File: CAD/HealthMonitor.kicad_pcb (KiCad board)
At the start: 2 copper layers, 20 x 30 mm, 28 parts, among them J1 USB_C_Receptacle_USB2.0, U1 ADP5092ACPZ-1-R7, U2 LTC4079IDD-PBF

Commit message: Finished PCB Draft -- waiting for review
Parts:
- added C10: 10µF, Capacitor_SMD:C_0402_1005Metric, F.Cu at (125.1, 111.9)
- added C11: 0.1µF, Capacitor_SMD:C_0402_1005Metric, F.Cu at (119.1, 118.9)
- added C12: 4.7µF, Capacitor_SMD:C_0402_1005Metric, F.Cu at (115.3, 117.0)
- added C13: 0.1µF, Capacitor_SMD:C_0402_1005Metric, F.Cu at (124.1, 120.1)
- added C14: 5600pF, Capacitor_SMD:C_0402_1005Metric, F.Cu at (122.3, 117.5)
- added C15: 10µF 10V, Capacitor_SMD:C_0402_1005Metric, F.Cu at (117.0, 123.0)
- added C16: 4.7µF, Capacitor_SMD:C_0402_1005Metric, F.Cu at (123.4, 118.6)
- added C17: 22u, Capacitor_SMD:C_0603_1608Metric, B.Cu at (105.0, 123.8)
- added C18: 12p, Capacitor_SMD:C_0402_1005Metric, F.Cu at (105.6, 107.6)
- added C19: 12p, Capacitor_SMD:C_0402_1005Metric, F.Cu at (105.6, 109.1)
- added C20: 1u, Capacitor_SMD:C_0402_1005Metric, F.Cu at (125.5, 105.4)
- added C21: 1u, Capacitor_SMD:C_0402_1005Metric, B.Cu at (115.6, 106.7)
- added C22: 0.1u, Capacitor_SMD:C_0402_1005Metric, B.Cu at (116.7, 106.7)
- added C23: 1u, Capacitor_SMD:C_0402_1005Metric, B.Cu at (112.8, 110.3)
- added C24: 1u, Capacitor_SMD:C_0402_1005Metric, F.Cu at (153.9, 126.5)
- added C25: 1u, Capacitor_SMD:C_0402_1005Metric, F.Cu at (153.2, 121.5)
- added C26: 1µf 10V, Capacitor_SMD:C_0402_1005Metric, F.Cu at (115.0, 120.2)
- added C27: 22u, Capacitor_SMD:C_0603_1608Metric, B.Cu at (105.0, 114.0)
- added C6: 4.7u, Capacitor_SMD:C_0402_1005Metric, F.Cu at (147.5, 106.8)
- added C7: 1u, Capacitor_SMD:C_0402_1005Metric, B.Cu at (118.9, 100.3)
- added C9: 100nF, Capacitor_SMD:C_0402_1005Metric, F.Cu at (125.1, 110.0)
- added D1: LED_ir, Diode_SMD:D_0603_1608Metric, B.Cu at (116.6, 103.9)
- added D2: LED_green, Diode_SMD:D_0603_1608Metric, B.Cu at (112.7, 100.9)
- added D3: LED_green, Diode_SMD:D_0603_1608Metric, B.Cu at (120.3, 100.9)
- added D4: SML-LX0404SIUPGUSB, SML-LX0404SIUPGUSB:DIOC0404X01-4N, F.Cu at (127.4, 105.5)
- added D5: LED-LT PWSG-AABB-36-46-F, LED_SMD:LED_PLCC-2, B.Cu at (108.4, 114.0)
- added D6: VEMD5010X01, footprints:VEMD5010X01, B.Cu at (106.1, 119.0)
- added D7: LED_LY_P47F-TM, LED_SMD:LED_PLCC-2, B.Cu at (108.4, 123.8)
- added D8: VEMD5010X01, footprints:VEMD5010X01, B.Cu at (110.6, 119.0)
- added J10: SDA, Connector_PinHeader_1.27mm:PinHeader_1x01_P1.27mm_Vertical, F.Cu at (141.9, 111.7)
- added J11: SCL, Connector_PinHeader_1.27mm:PinHeader_1x01_P1.27mm_Vertical, F.Cu at (141.9, 110.2)
- added J12: DIS_SW, Connector_PinHeader_1.27mm:PinHeader_1x01_P1.27mm_Vertical, F.Cu at (141.9, 113.0)
- added J13: BAT_CHRG, Connector_PinHeader_1.27mm:PinHeader_1x01_P1.27mm_Vertical, F.Cu at (141.9, 114.5)
- added J14: USBDP, Connector_PinHeader_1.27mm:PinHeader_1x01_P1.27mm_Vertical, F.Cu at (143.8, 115.2)
- added J15: USBDM, Connector_PinHeader_1.27mm:PinHeader_1x01_P1.27mm_Vertical, F.Cu at (143.8, 116.5)
- added J16: USB_V, Connector_PinHeader_1.27mm:PinHeader_1x01_P1.27mm_Vertical, F.Cu at (141.9, 115.8)
- added J17: VBUS, Connector_PinHeader_1.27mm:PinHeader_1x01_P1.27mm_Vertical, F.Cu at (129.0, 114.2)
- added J18: D+, Connector_PinHeader_1.27mm:PinHeader_1x01_P1.27mm_Vertical, F.Cu at (129.0, 115.6)
- added J19: D-, Connector_PinHeader_1.27mm:PinHeader_1x01_P1.27mm_Vertical, F.Cu at (129.0, 117.0)
- added J2: TEG+, Connector_PinHeader_1.27mm:PinHeader_1x01_P1.27mm_Vertical, F.Cu at (141.9, 100.5)
- added J20: SDA, Connector_PinHeader_1.27mm:PinHeader_1x01_P1.27mm_Vertical, F.Cu at (129.0, 110.0)
- added J21: SCL, Connector_PinHeader_1.27mm:PinHeader_1x01_P1.27mm_Vertical, F.Cu at (129.0, 108.6)
- added J22: VCC, Connector_PinHeader_1.27mm:PinHeader_1x01_P1.27mm_Vertical, F.Cu at (130.3, 106.7)
- added J23: GND, Connector_PinHeader_1.27mm:PinHeader_1x01_P1.27mm_Vertical, F.Cu at (130.3, 105.3)
- added J24: BAT_CHRG, Connector_PinHeader_1.27mm:PinHeader_1x01_P1.27mm_Vertical, F.Cu at (129.0, 112.8)
- added J25: DIS_SW, Connector_PinHeader_1.27mm:PinHeader_1x01_P1.27mm_Vertical, F.Cu at (129.0, 111.4)
- added J3: TEG-, Connector_PinHeader_1.27mm:PinHeader_1x01_P1.27mm_Vertical, F.Cu at (141.9, 101.8)
- added J4: BAT-, Connector_PinHeader_1.27mm:PinHeader_1x01_P1.27mm_Vertical, F.Cu at (141.9, 106.0)
- added J5: BAT+, Connector_PinHeader_1.27mm:PinHeader_1x01_P1.27mm_Vertical, F.Cu at (141.9, 103.2)
- added J6: USB_C_Receptacle_USB2.0, Connector_USB:USB_C_Receptacle_Amphenol_12401610E4-2A_CircularHoles, F.Cu at (144.9, 123.0)
- added J7: Conn_02x05_Odd_Even, Connector_PinHeader_1.27mm:PinHeader_2x05_P1.27mm_Vertical, F.Cu at (127.0, 98.0)
- added J8: VCC, Connector_PinHeader_1.27mm:PinHeader_1x01_P1.27mm_Vertical, F.Cu at (141.9, 108.8)
- added J9: GND, Connector_PinHeader_1.27mm:PinHeader_1x01_P1.27mm_Vertical, F.Cu at (141.9, 107.5)
- added L2: 4.7µH, Inductor_SMD:L_0603_1608Metric, F.Cu at (122.9, 116.1)
- added R19: 3.32M, Resistor_SMD:R_0402_1005Metric, F.Cu at (156.2, 107.6)
- added R20: 2.4k, Resistor_SMD:R_0402_1005Metric, F.Cu at (151.9, 116.7)
- added R21: 6.65M, Resistor_SMD:R_0402_1005Metric, F.Cu at (158.2, 107.6)
- added R22: 412k, Resistor_SMD:R_0402_1005Metric, F.Cu at (151.9, 118.2)
- added R23: 10k, Resistor_SMD:R_0402_1005Metric, B.Cu at (117.0, 99.0)
- added R24: 10k, Resistor_SMD:R_0402_1005Metric, B.Cu at (117.0, 97.8)
- added R25: 10k, Resistor_SMD:R_0402_1005Metric, B.Cu at (114.1, 100.4)
- added R26: 50k, Resistor_SMD:R_0402_1005Metric, F.Cu at (121.4, 118.6)
- added R27: 50k, Resistor_SMD:R_0402_1005Metric, F.Cu at (125.4, 121.0)
- added R28: 50k, Resistor_SMD:R_0402_1005Metric, F.Cu at (124.3, 122.5)
- added R29: 50k, Resistor_SMD:R_0402_1005Metric, F.Cu at (123.1, 122.9)
- added R30: 50k, Resistor_SMD:R_0402_1005Metric, F.Cu at (122.0, 123.0)
- added R31: 4.75k, Resistor_SMD:R_0402_1005Metric, F.Cu at (120.8, 117.0)
- added R32: 10k, Resistor_SMD:R_0402_1005Metric, F.Cu at (105.3, 105.4)
- added R33: 10k, Resistor_SMD:R_0402_1005Metric, F.Cu at (104.5, 98.3)
- added R34: 6.6k, Resistor_SMD:R_0402_1005Metric, F.Cu at (127.5, 106.8)
- added R35: 10k, Resistor_SMD:R_0402_1005Metric, F.Cu at (147.3, 111.1)
- added R36: 0, Resistor_SMD:R_0603_1608Metric, F.Cu at (130.9, 108.8)
- added Rpu1: 10kOhms, Resistor_SMD:R_0402_1005Metric, F.Cu at (123.6, 107.7)
- added Rpu2: 10kOhms, Resistor_SMD:R_0402_1005Metric, F.Cu at (122.6, 107.7)
- added U10: AT24CS02-XHM, Package_SO:TSSOP-8_4.4x3mm_P0.65mm, F.Cu at (106.9, 100.8)
- added U11: BT832L, footprints:BT832-BT832L, F.Cu at (109.8, 106.2)
- added U12: CP2102N-A01-GQFN24, Package_DFN_QFN:QFN-24-1EP_4x4mm_P0.5mm_EP2.6x2.6mm, B.Cu at (116.8, 110.4)
- added U13: ADG884BRMZ, footprints:ADG884BRMZ, F.Cu at (149.8, 113.6)
- added U3: LTC4079IDD-PBF, footprints:LTC4079IDD-PBF, F.Cu at (155.4, 118.5)
- added U4: LD39015M33R, Package_TO_SOT_SMD:SOT-23-5, F.Cu at (153.4, 124.0)
- added U5: BH1792GLC, BH1790GLC-E2:PQFN70P280X280X100-10N, B.Cu at (116.5, 101.1)
- added U6: LSM6DS33TR, LSM6DS33TR:PQFN50P300X300X86-16N, F.Cu at (122.7, 110.8)
- added U7: TXB0104RUT, Package_DFN_QFN:Texas_R_PUQFN-N12, F.Cu at (120.3, 120.6)
- added U8: MAX1921EUT18+, footprints:MAX1921EUT18&plus_T, F.Cu at (118.0, 116.5)
- added U9: MAX86141ENP+, footprints:MAX86141ENP, F.Cu at (116.8, 120.6)
- added Y1: ABS06-32.768KHZ-T, ABS06-32.768KHZ-T:XTAL_ABS06-32.768KHZ-T, F.Cu at (107.7, 108.3)
- C1: value 10u -> 0.1u
- C3: value 10n -> 10u
- C4: value 1u -> 10n
- C5: value 4.7u -> 1u
- J1: value USB_C_Receptacle_USB2.0 -> BAT_T; footprint Connector_USB:USB_C_Receptacle_Amphenol_12401610E4-2A_CircularHoles -> Connector_PinHeader_1.27mm:PinHeader_1x01_P1.27mm_Vertical
- R10: value 3.01M -> 10k
- R11: value 6.98M -> 10k
- R12: value 3.32M -> 5M
- R13: value 6.65M -> 5M
- R14: value 1.07M -> 3.01M
- R15: value 3.57M -> 6.98M
- R16: value 2.4k -> 3.32M
- R17: value 6.49M -> 6.65M
- R18: value 412k -> 1.07M
- R6: value 3.3k -> 1M
- R7: value 10k -> 2M
- R8: value 5M -> 3.3k
- R9: value 5M -> 10k
- U1: value ADP5092ACPZ-1-R7 -> MAX17048G+T10; footprint footprints:ADP5092ACPZ-1-R7 -> footprints:MAX17048G+
- U2: value LTC4079IDD-PBF -> ADP5092ACPZ-1-R7; footprint footprints:LTC4079IDD-PBF -> footprints:ADP5092ACPZ-1-R7
- moved C5 54.5 mm to (158.7, 120.0), turned to 0 degrees
- moved C1 51.4 mm to (155.9, 115.2), turned to 0 degrees
- moved U1 47.1 mm to (156.2, 113.0), turned to 90 degrees
- moved R17 46.0 mm to (158.0, 104.1)
- moved R14 45.1 mm to (156.3, 101.8), turned to 0 degrees
- moved R8 44.8 mm to (158.7, 119.0)
- moved R13 44.7 mm to (158.2, 106.6)
- moved C2 44.6 mm to (149.2, 102.1), turned to 270 degrees
- moved R15 44.5 mm to (158.2, 102.6), turned to 180 degrees
- moved R10 44.4 mm to (156.2, 110.0), turned to 270 degrees
- moved C4 44.2 mm to (152.2, 101.6), turned to 90 degrees
- moved R3 44.0 mm to (150.8, 102.1)
- moved R9 43.3 mm to (158.4, 117.5)
- moved L1 43.3 mm to (147.8, 103.1), turned to 90 degrees
- moved R1 42.9 mm to (150.8, 101.1)
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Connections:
- C1 pad 1: /power/TEG+ -> GND
- C1 pad 2: GND -> /power/BAT+
- C2 pad 1: +3V3 -> /power/TEG+
- C3 pad 1: Net-(C3-Pad1) -> /power/EH_3v3
- C5 pad 1: GND -> /power/USB_VBUS
- C5 pad 2: Net-(C5-Pad2) -> GND
- R10 pad 1: GND -> +3V3
- R10 pad 2: Net-(R10-Pad2) -> /SCL
- R11 pad 1: /power/REF -> +3V3
- R11 pad 2: Net-(R10-Pad2) -> /SDA
- R14 pad 1: Net-(R14-Pad1) -> GND
- R14 pad 2: /power/BAT+ -> Net-(R14-Pad2)
- R15 pad 1: GND -> /power/REF
- R15 pad 2: Net-(R15-Pad2) -> Net-(R14-Pad2)
- R16 pad 1: +3V3 -> GND
- R16 pad 2: /power/BAT_CHRG -> Net-(R16-Pad2)
- R17 pad 2: Net-(R15-Pad2) -> Net-(R16-Pad2)
- R18 pad 2: Net-(R14-Pad1) -> /power/BAT_USB
- R6 pad 1: Net-(R6-Pad1) -> /power/USB_VBUS
- R6 pad 2: GND -> /power/B_CONN
- R7 pad 1: Net-(R7-Pad1) -> /power/B_CONN
- R7 pad 2: /power/BAT_T -> GND
- R8 pad 1: GND -> Net-(R8-Pad1)
- R8 pad 2: Net-(R8-Pad2) -> GND
- R9 pad 1: /power/REF -> Net-(R9-Pad1)
- R9 pad 2: Net-(R8-Pad2) -> /power/BAT_T
- U1 pad 1: /power/REF -> GND
- U1 pad 2: Net-(R15-Pad2) -> /power/BAT+
- U1 pad 3: Net-(R8-Pad2) -> /power/BAT+
- U1 pad 4: Net-(R4-Pad1) -> GND
- U1 pad 5: Net-(R12-Pad2) -> Net-(U1-Pad5)
- U1 pad 6: Net-(R10-Pad2) -> GND
- U1 pad 7: GND -> /SCL
- U1 pad 8: Net-(C3-Pad1) -> /SDA
- U1 pad 9: Net-(R1-Pad2) -> GND
- U2 pad 1: Net-(C4-Pad1) -> /power/REF
- U2 pad 10: /power/BAT+ -> /power/TEG+
- U2 pad 11: GND -> /power/REG_GOOD
- U2 pad 2: Net-(C4-Pad1) -> Net-(R19-Pad2)
- U2 pad 3: Net-(R6-Pad1) -> Net-(R12-Pad2)
- U2 pad 4: Net-(R7-Pad1) -> Net-(R4-Pad1)
- U2 pad 5: /power/BAT_T -> Net-(R16-Pad2)
- U2 pad 6: GND -> Net-(R14-Pad2)
- U2 pad 7: /power/BAT_CHRG -> GND
- U2 pad 8: Net-(R18-Pad1) -> Net-(C4-Pad1)
- U2 pad 9: Net-(R14-Pad1) -> Net-(R1-Pad2)
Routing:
- net +3V3: track 25.3 -> 196.8 mm, vias 2 -> 13
- net GND: track 13.2 -> 111.9 mm, vias 2 -> 17
- net /power/USB_VBUS: track 0.00 -> 62.8 mm, vias 0 -> 1
- net /SDA: track 0.00 -> 59.2 mm, vias 0 -> 3
- net Net-(D6-Pad3): track 0.00 -> 55.2 mm, vias 0 -> 2
- net /SCL: track 0.00 -> 54.5 mm, vias 0 -> 6
- net /DIS_SW: track 0.00 -> 47.3 mm, vias 0 -> 1
- net /BAT_CHRG: track 0.00 -> 40.4 mm, vias 0 -> 2
- net /SoC/SDI: track 0.00 -> 38.3 mm, vias 0 -> 2
- net /programmer/D-: track 0.00 -> 37.8 mm, vias 0 -> 2
- net /programmer/D+: track 0.00 -> 36.5 mm, vias 0 -> 2
- net /SoC/SCLK: track 0.00 -> 35.6 mm, vias 0 -> 3
- net /SoC/SDO: track 0.00 -> 34.1 mm, vias 0 -> 2
- net /SoC/CSB: track 0.00 -> 29.0 mm, vias 0 -> 2
- net /power/BAT_T: track 3.01 -> 25.9 mm, vias 0 -> 1
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- added copper zone on B.Cu, net Net-(D6-Pad3)
- added copper zone on F.Cu, net Net-(D6-Pad3)
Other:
- board size 20 x 30 mm -> 58.7 x 33.3 mm
- net class Default: via_dia 0.8 -> 0.6; via_drill 0.4 -> 0.3
- rule trace_min: 0.2 -> 0.1

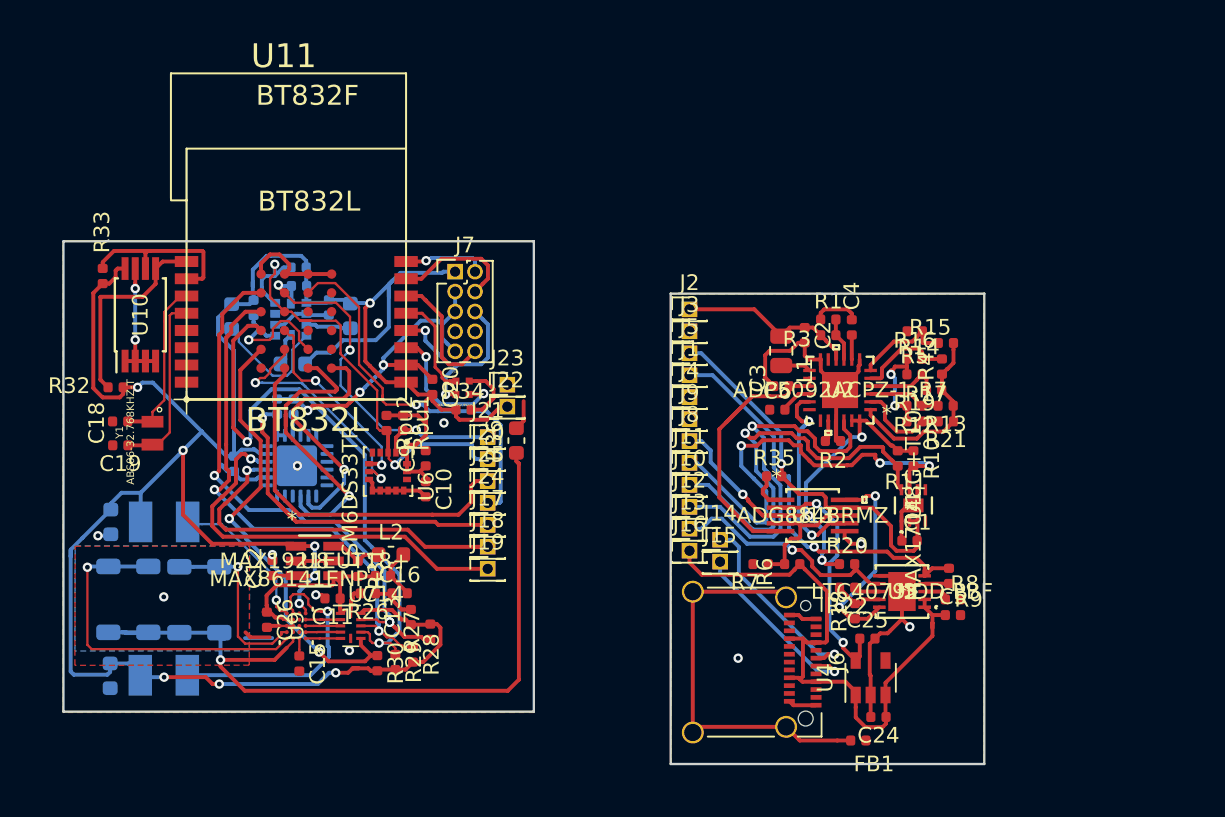
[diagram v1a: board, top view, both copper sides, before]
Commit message: Fixed most DRC errors, remaining errors should be fine
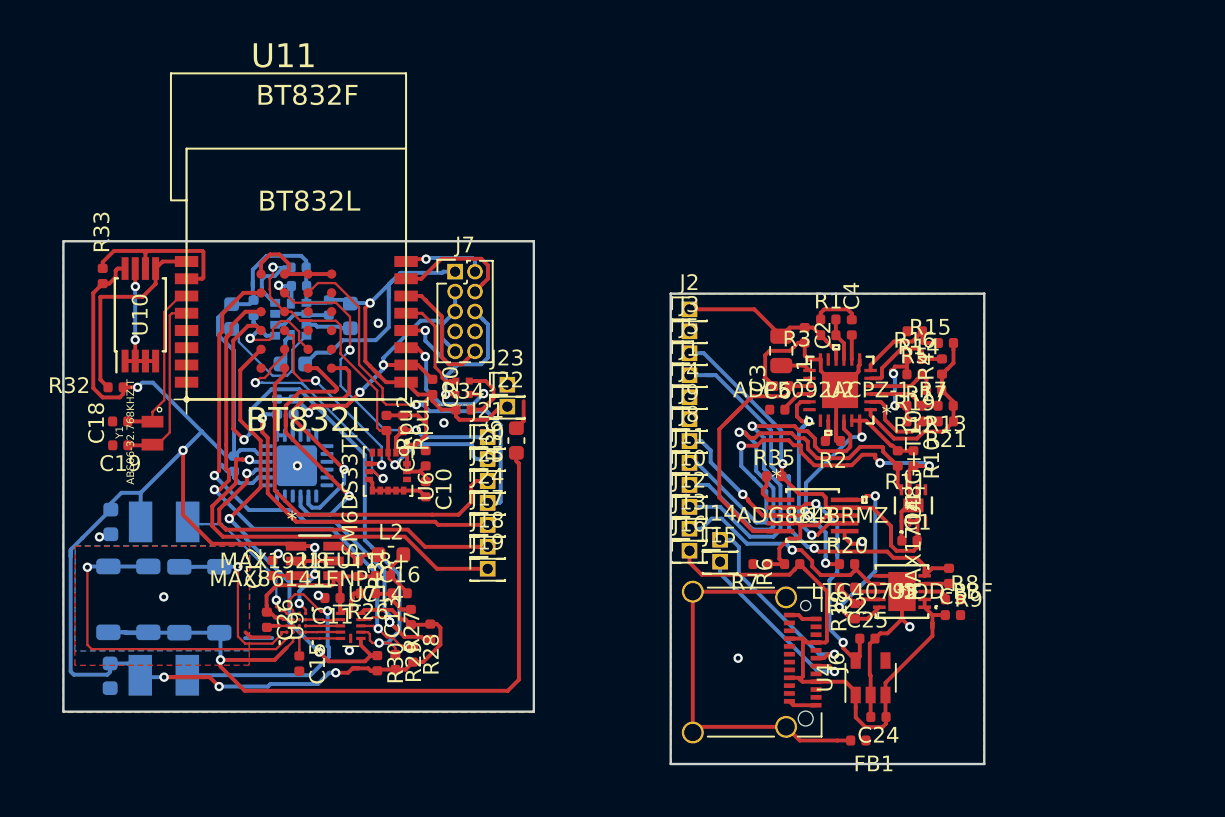
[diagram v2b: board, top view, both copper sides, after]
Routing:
- net +3V3: track 196.8 -> 199.6 mm
- net /SDA: track 59.2 -> 60.4 mm
- net /power/USB_3v3: track 15.9 -> 16.8 mm
- net /power/BAT_T: track 25.9 -> 26.5 mm
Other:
- rule trace_min: 0.1 -> 0.15
- rule via_min_size: 0.4 -> 0.3

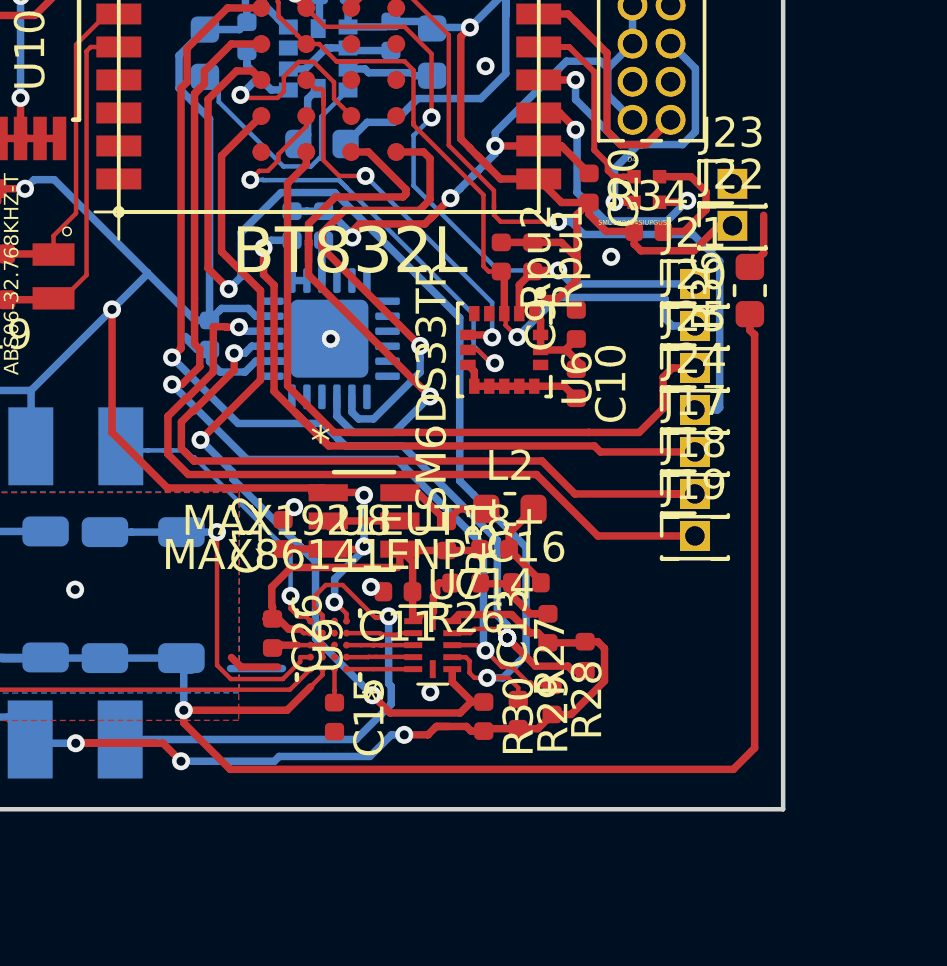
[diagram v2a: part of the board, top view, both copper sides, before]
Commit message: Moved test point to reduce the length of the LED lead
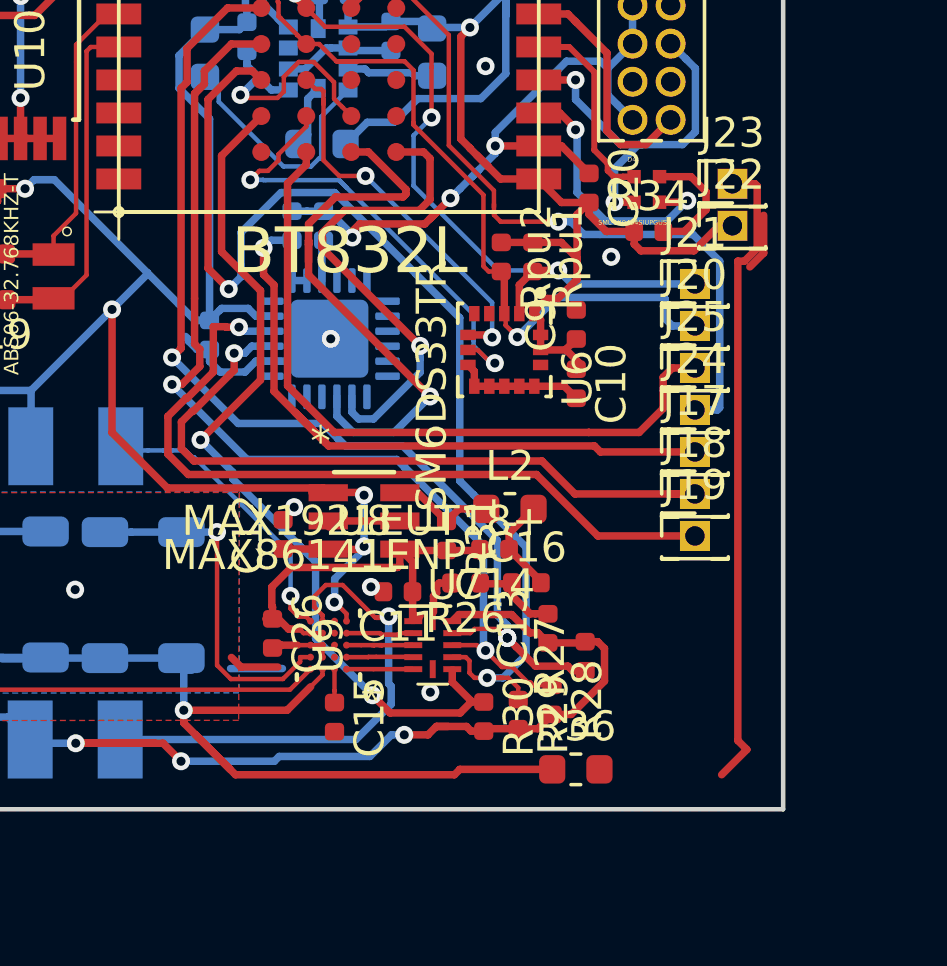
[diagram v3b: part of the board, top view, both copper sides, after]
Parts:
- moved R36 17.0 mm to (125.1, 124.8), turned to 0 degrees
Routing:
- net GND: track 112.0 -> 133.4 mm
- net Net-(D6-Pad3): track 55.2 -> 35.4 mm
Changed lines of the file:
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@@
     (thickness 1.6)
     (drawings 8)
-    (tracks 1429)
+    (tracks 1436)
     (zones 0)
     (modules 114)
@@
   )
   (module Resistor_SMD:R_0603_1608Metric (layer F.Cu)
-    (at 130.86 108.82 90)
+    (at 125.06 124.78)
     (descr "Resistor SMD 0603 (1608 Metric), square (rectangular) end terminal, IPC_7351 nominal, (Body size source: http://www.tortai-tech.com/upload/download/2011102023233369053.pdf), generated with kicad-footprint-generator")
     (tags resistor)
     (attr smd)
-    (fp_text reference R36 (at 0 -1.43 90) (layer F.SilkS)
+    (fp_text reference R36 (at 0 -1.43) (layer F.SilkS)
       (effects (font (size 1 1) (thickness 0.15)))
     )
-    (fp_text value 0 (at 0 1.43 90) (layer F.Fab)
+    (fp_text value 0 (at 0 1.43) (layer F.Fab)
       (effects (font (size 1 1) (thickness 0.15)))
     )
@@
     (fp_line (start 1.48 -0.73) (end 1.48 0.73) (layer F.CrtYd) (width 0.05))
     (fp_line (start 1.48 0.73) (end -1.48 0.73) (layer F.CrtYd) (width 0.05))
-    (fp_text user %R (at 0 0 90) (layer F.Fab)
+    (fp_text user %R (at 0 0) (layer F.Fab)
       (effects (font (size 0.4 0.4) (thickness 0.06)))
     )
-    (pad 1 smd roundrect (at -0.7875 0 90) (size 0.875 0.95) (layers F.Cu F.Paste F.Mask) (roundrect_rratio 0.25)
+    (pad 1 smd roundrect (at -0.7875 0) (size 0.875 0.95) (layers F.Cu F.Paste F.Mask) (roundrect_rratio 0.25)
       (net 119 "Net-(D6-Pad3)"))
-    (pad 2 smd roundrect (at 0.7875 0 90) (size 0.875 0.95) (layers F.Cu F.Paste F.Mask) (roundrect_rratio 0.25)
+    (pad 2 smd roundrect (at 0.7875 0) (size 0.875 0.95) (layers F.Cu F.Paste F.Mask) (roundrect_rratio 0.25)
       (net 3 GND))
     (model ${KISYS3DMOD}/Resistor_SMD.3dshapes/R_0603_1608Metric.wrl
@@
   (segment (start 115.67 116.095) (end 115.3 116.465) (width 0.25) (layer F.Cu) (net 3))
   (segment (start 115.67 116.02) (end 115.67 116.095) (width 0.25) (layer F.Cu) (net 3))
+  (segment (start 131.03 105.26) (end 130.28 105.26) (width 0.25) (layer F.Cu) (net 3))
+  (segment (start 131.105001 105.335001) (end 131.03 105.26) (width 0.25) (layer F.Cu) (net 3))
+  (segment (start 130.76 124.12) (end 130.46 123.82) (width 0.25) (layer F.Cu) (net 3))
+  (segment (start 129.92 124.96) (end 130.76 124.12) (width 0.25) (layer F.Cu) (net 3))
+  (segment (start 130.46 123.82) (end 130.46 107.84) (width 0.25) (layer F.Cu) (net 3))
+  (segment (start 131.105001 107.416611) (end 131.105001 105.335001) (width 0.25) (layer F.Cu) (net 3))
+  (segment (start 130.46 107.84) (end 130.681612 107.84) (width 0.25) (layer F.Cu) (net 3))
+  (segment (start 130.681612 107.84) (end 131.105001 107.416611) (width 0.25) (layer F.Cu) (net 3))
   (segment (start 154.0046 118.949999) (end 152.950001 118.949999) (width 0.25) (layer F.Cu) (net 4))
   (segment (start 151.465 118.465) (end 151.465 118.2) (width 0.25) (layer F.Cu) (net 4))
@@
   (segment (start 116.22 122.027002) (end 115.437002 122.81) (width 0.25) (layer F.Cu) (net 119))
   (segment (start 115.437002 122.81) (end 111.99 122.81) (width 0.25) (layer F.Cu) (net 119))
-  (segment (start 130.995 110.28) (end 130.86 110.145) (width 0.25) (layer F.Cu) (net 119))
-  (segment (start 113.535736 124.78) (end 130.31 124.78) (width 0.25) (layer F.Cu) (net 119))
-  (segment (start 130.86 110.145) (end 130.86 109.6075) (width 0.25) (layer F.Cu) (net 119))
-  (segment (start 130.31 124.78) (end 131.02 124.07) (width 0.25) (layer F.Cu) (net 119))
-  (segment (start 131.02 110.28) (end 130.995 110.28) (width 0.25) (layer F.Cu) (net 119))
-  (segment (start 131.02 124.07) (end 131.02 110.28) (width 0.25) (layer F.Cu) (net 119))
   (segment (start 111.99 122.81) (end 111.99 123.234264) (width 0.25) (layer F.Cu) (net 119))
-  (segment (start 111.99 123.234264) (end 113.535736 124.78) (width 0.25) (layer F.Cu) (net 119))
+  (segment (start 113.715736 124.96) (end 112.375736 123.62) (width 0.25) (layer F.Cu) (net 119))
+  (segment (start 121.0125 124.96) (end 113.715736 124.96) (width 0.25) (layer F.Cu) (net 119))
+  (segment (start 111.99 123.234264) (end 112.375736 123.62) (width 0.25) (layer F.Cu) (net 119))
+  (segment (start 112.375736 123.62) (end 113.535736 124.78) (width 0.25) (layer F.Cu) (net 119))
+  (segment (start 121.1925 124.78) (end 124.2725 124.78) (width 0.25) (layer F.Cu) (net 119))
+  (segment (start 121.0125 124.96) (end 121.1925 124.78) (width 0.25) (layer F.Cu) (net 119))
   (zone (net 3) (net_name GND) (layer F.Cu) (hatch edge 0.508)
     (connect_pads (clearance 0.2))

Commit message: Generated gerbers
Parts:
- J6: footprint Connector_USB:USB_C_Receptacle_Amphenol_12401610E4-2A_CircularHoles -> footprints:USB_C_Receptacle_Amphenol_12401610E4-2A_CircularHoles
- moved C24 11.8 mm to (165.2, 123.1)
- moved C25 11.8 mm to (164.5, 118.1)
- moved C5 11.8 mm to (170.0, 116.6)
- moved FB1 11.8 mm to (163.9, 124.6)
- moved J1 11.8 mm to (153.2, 101.3)
- moved J10 11.8 mm to (153.2, 108.3)
- moved J11 11.8 mm to (153.2, 106.9)
- moved J12 11.8 mm to (153.2, 109.7)
- moved J13 11.8 mm to (153.2, 111.1)
- moved J14 11.8 mm to (155.1, 111.8)
- moved J15 11.8 mm to (155.1, 113.2)
- moved J2 11.8 mm to (153.2, 97.1)
- moved J4 11.8 mm to (153.2, 102.7)
- moved J5 11.8 mm to (153.2, 99.9)
- moved J6 11.8 mm to (156.2, 119.6)
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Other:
- board size 58.7 x 33.3 mm -> 70 x 30 mm
